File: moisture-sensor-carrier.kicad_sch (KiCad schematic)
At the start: 57 parts, among them J1 USB-C receptacle, J2 Battery - Adafruit 1578, J3 Solar panel, J4 SWD 10p 1.27mm, J5 Antenna feed, U1 nRF54L15-QFAA, U2 nPM1300-QEAA, U3 FDC1004, U4 SHT45-AD1F, X1 CM8V-T1A 32.768kHz CL=7pF 20p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, X2 FA-128 32MHz CL=8pF

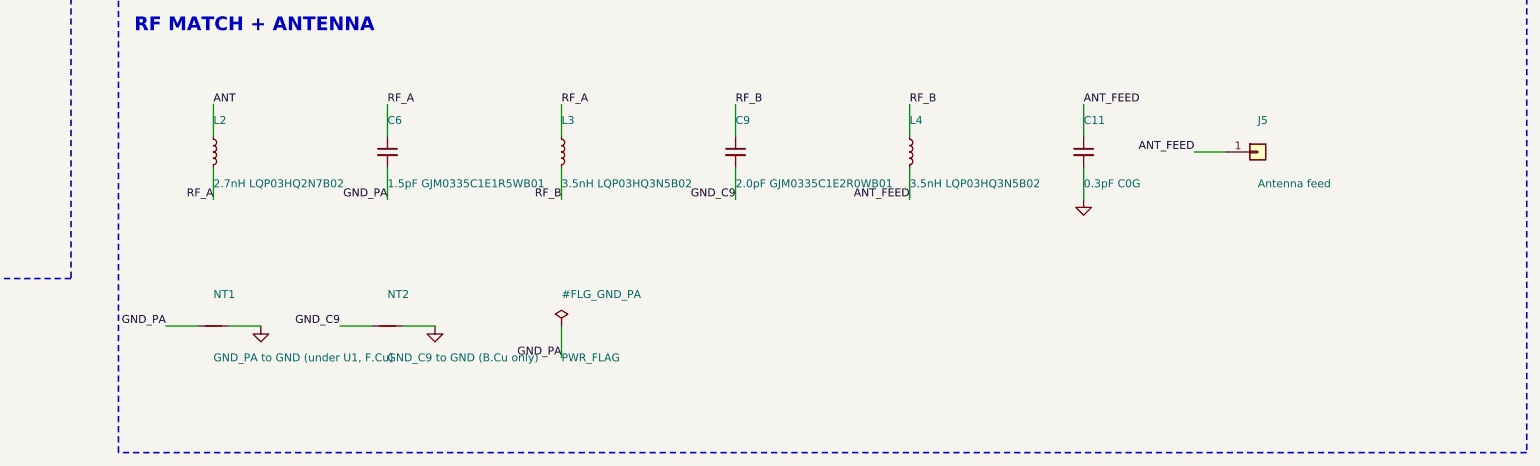
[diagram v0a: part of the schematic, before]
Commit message: Correct the stackup: order plain JLC04161H-7628, not 7628D. Remove J5.
Stackup, re-read against JLCPCB's own published list (Controlled Impedance PCB
Layer Stackup, filtered to 1.6 mm / 1oz outer / 0.5oz inner):

LAYOUT.md said 7628D was the ONLY 4-layer 7628 variant with a single 0.21040 mm
prepreg under the top layer. That is wrong - THREE of the eighteen entries have
it: the default "No requirement Stackup", plain JLC04161H-7628, and 7628D. The
first two have a 1.065 mm core and sum to 1.586 mm, a real 1.6 mm board. 7628D
has a 1.265 mm core and sums to 1.786 mm.

That is exactly what the open "confirm the total thickness" question in
NEXT-STEPS.md was detecting - 7628D was never going to be 1.6 mm. All three give
identical impedance because the top dielectric is the same, so plain 7628 is
strictly better: right thickness, and it is also JLC's cheapest and quickest
option. B/C/E/F stay out at 0.43-0.65 mm under the top layer.

The 1.265 mm core in LAYOUT.md belonged to 7628D. Reverted to 1.065 mm in the
stackup table and in the section 5 guard-capacitance figures (3.82e-8 F/m^2,
105 cm^2 to reach the FDC1004's 400 pF shield limit - still 5x the ~20 cm^2 the
probe guard actually uses, so no design impact). The board file's 1.065 mm was
right all along; the docs were the thing that had drifted.

Re-checked the 0.38 mm trace against JLCPCB's published material parameters,
which the hand calculation used none of: 7628 er = 4.4 (not the 4.2 assumed),
solder mask er 3.8 at 0.6 mil above the trace, and an etch taper of
top width = base - 0.7 mil.

  er 4.2 bare            49.9 ohm   <- what LAYOUT.md solved
  er 4.4 bare            48.8 ohm
  er 4.4 + mask          48.2 ohm
  er 4.4 + etch taper    49.5 ohm

Mask and taper push opposite ways and largely cancel. 0.38 mm lands at roughly
48.5-49.5 ohm on JLC's own material - VSWR 1.03, about 0.01 dB. No respin.
Order with impedance control and let them solve the real pressed stackup.

Also corrected: LAYOUT.md's "stitchin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
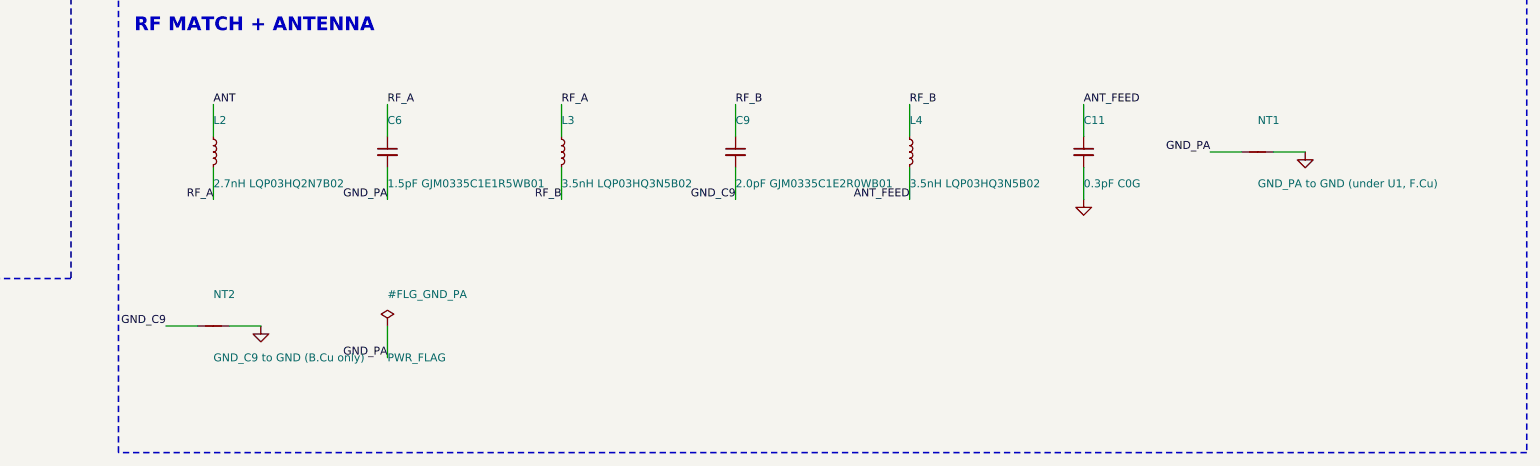
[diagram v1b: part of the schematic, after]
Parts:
- removed J5: Antenna feed, TestPoint:TestPoint_Pad_D1.0mm, symbol Connector_Generic:Conn_01x01
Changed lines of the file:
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@@
 		(stroke (width 0) (type default))
 	)
-	(wire (pts (xy 530.86 342.9) (xy 525.78 342.9))
+	(wire (pts (xy 533.4000000000001 342.9) (xy 528.32 342.9))
 		(stroke (width 0) (type default))
 	)
-	(wire (pts (xy 365.76 370.84) (xy 360.68 370.84))
+	(wire (pts (xy 538.48 342.9) (xy 543.5600000000001 342.9))
 		(stroke (width 0) (type default))
 	)
-	(wire (pts (xy 370.84000000000003 370.84) (xy 375.92 370.84))
-		(stroke (width 0) (type default))
-	)
-	(wire (pts (xy 393.7 370.84) (xy 388.62 370.84))
+	(wire (pts (xy 365.76 370.84) (xy 360.68 370.84))
 		(stroke (width 0) (type default))
 	)
-	(wire (pts (xy 398.78000000000003 370.84) (xy 403.86 370.84))
+	(wire (pts (xy 370.84000000000003 370.84) (xy 375.92 370.84))
 		(stroke (width 0) (type default))
 	)
@@
 		(stroke (width 0) (type default))
 	)
-	(wire (pts (xy 424.18 370.84) (xy 424.18 375.91999999999996))
+	(wire (pts (xy 396.24 370.84) (xy 396.24 375.91999999999996))
 		(stroke (width 0) (type default))
 	)
@@
 		(effects (font (size 1.27 1.27)) (justify left bottom))
 	)
-	(label "ANT_FEED"
-		(at 525.78 342.9 0)
-		(fields_autoplaced yes)
-		(effects (font (size 1.27 1.27)) (justify right bottom))
-	)
 	(label "GND_PA"
-		(at 360.68 370.84 0)
+		(at 528.32 342.9 0)
 		(fields_autoplaced yes)
 		(effects (font (size 1.27 1.27)) (justify right bottom))
 	)
 	(label "GND_C9"
-		(at 388.62 370.84 0)
+		(at 360.68 370.84 0)
 		(fields_autoplaced yes)
 		(effects (font (size 1.27 1.27)) (justify right bottom))
@@
 	)
 	(label "GND_PA"
-		(at 424.18 375.91999999999996 0)
+		(at 396.24 375.91999999999996 0)
 		(fields_autoplaced yes)
 		(effects (font (size 1.27 1.27)) (justify right bottom))
@@
 	)
 	(symbol
-		(lib_id "Connector_Generic:Conn_01x01")
-		(at 535.94 342.9 0)
-		(unit 1)
-		(exclude_from_sim no)
-		(in_bom yes)
-		(on_board yes)
-		(dnp no)
-		(fields_autoplaced yes)
-		(property "Reference" "J5"
-			(at 535.94 337.82 0)
-			(effects (font (size 1.27 1.27)) (justify left))
-		)
-		(property "Value" "Antenna feed"
-			(at 535.94 347.98 0)
-			(effects (font (size 1.27 1.27)) (justify left))
-		)
-		(property "Footprint" "TestPoint:TestPoint_Pad_D1.0mm"
-			(at 535.94 342.9 0)
-			(effects (font (size 1.27 1.27)) (hide yes))
-		)
-		(pin "1")
-		(instances
-			(project "moisture-sensor-carrier"
-				(path "/29551000-a13a-494c-a3a3-b85b9fc11a3c"
-					(reference "J5")
-					(unit 1)
-				)
-			)
-		)
-	)
-	(symbol
 		(lib_id "Device:NetTie_2")
-		(at 368.3 370.84 0)
+		(at 535.94 342.9 0)
 		(unit 1)
 		(exclude_from_sim no)
@@
 		(fields_autoplaced yes)
 		(property "Reference" "NT1"
-			(at 368.3 365.76 0)
+			(at 535.94 337.82 0)
 			(effects (font (size 1.27 1.27)) (justify left))
 		)
 		(property "Value" "GND_PA to GND (under U1, F.Cu)"
-			(at 368.3 375.92 0)
+			(at 535.94 347.98 0)
 			(effects (font (size 1.27 1.27)) (justify left))
 		)
 		(property "Footprint" "footprints:NetTie_VSSPA"
-			(at 368.3 370.84 0)
+			(at 535.94 342.9 0)
 			(effects (font (size 1.27 1.27)) (hide yes))
 		)
@@
 	(symbol
 		(lib_id "power:GND")
-		(at 375.92 370.84 0)
+		(at 543.5600000000001 342.9 0)
 		(unit 1)
 		(exclude_from_sim no)
@@
 		(dnp no)
 		(property "Reference" "#PWR039"
-			(at 375.92 370.84 0)
+			(at 543.5600000000001 342.9 0)
 			(effects (font (size 1.27 1.27)) (hide yes))
 		)
 		(property "Value" "GND"
-			(at 375.92 374.34 0)
+			(at 543.5600000000001 346.4 0)
 			(effects (font (size 1.27 1.27)) (hide yes))
 		)
@@
 	(symbol
 		(lib_id "Device:NetTie_2")
-		(at 396.24 370.84 0)
+		(at 368.3 370.84 0)
 		(unit 1)
 		(exclude_from_sim no)
@@
 		(fields_autoplaced yes)
 		(property "Reference" "NT2"
-			(at 396.24 365.76 0)
+			(at 368.3 365.76 0)
 			(effects (font (size 1.27 1.27)) (justify left))
 		)
 		(property "Value" "GND_C9 to GND (B.Cu only)"
-			(at 396.24 375.92 0)
+			(at 368.3 375.92 0)
 			(effects (font (size 1.27 1.27)) (justify left))
 		)
 		(property "Footprint" "NetTie:NetTie-2_SMD_Pad0.5mm"
-			(at 396.24 370.84 0)
+			(at 368.3 370.84 0)
 			(effects (font (size 1.27 1.27)) (hide yes))
 		)
@@
 	(symbol
 		(lib_id "power:GND")
-		(at 403.86 370.84 0)
+		(at 375.92 370.84 0)
 		(unit 1)
 		(exclude_from_sim no)
@@
 		(dnp no)
 		(property "Reference" "#PWR040"
-			(at 403.86 370.84 0)
+			(at 375.92 370.84 0)
 			(effects (font (size 1.27 1.27)) (hide yes))
 		)
 		(property "Value" "GND"
-			(at 403.86 374.34 0)
+			(at 375.92 374.34 0)
 			(effects (font (size 1.27 1.27)) (hide yes))
 		)
@@
 	(symbol
 		(lib_id "power:PWR_FLAG")
-		(at 424.18 370.84 0)
+		(at 396.24 370.84 0)
 		(unit 1)
 		(exclude_from_sim no)
@@
 		(fields_autoplaced yes)
 		(property "Reference" "#FLG_GND_PA"
-			(at 424.18 365.76 0)
+			(at 396.24 365.76 0)
 			(effects (font (size 1.27 1.27)) (justify left))
 		)
 		(property "Value" "PWR_FLAG"
-			(at 424.18 375.92 0)
+			(at 396.24 375.92 0)
 			(effects (font (size 1.27 1.27)) (justify left))
 		)
 		(property "Footprint" ""
-			(at 424.18 370.84 0)
+			(at 396.24 370.84 0)
 			(effects (font (size 1.27 1.27)) (hide yes))
 		)
